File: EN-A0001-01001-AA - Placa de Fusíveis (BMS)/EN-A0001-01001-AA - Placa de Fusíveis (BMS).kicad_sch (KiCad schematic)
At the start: 10 parts

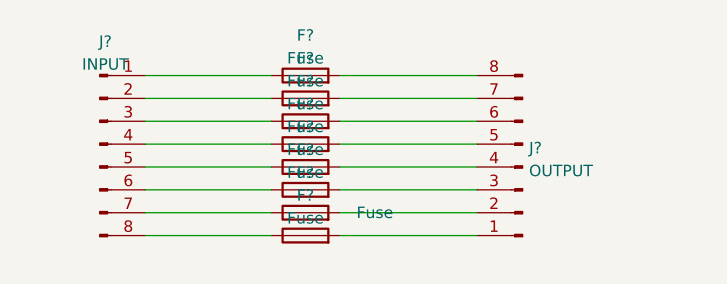
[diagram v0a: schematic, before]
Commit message: ADD: fusiveis
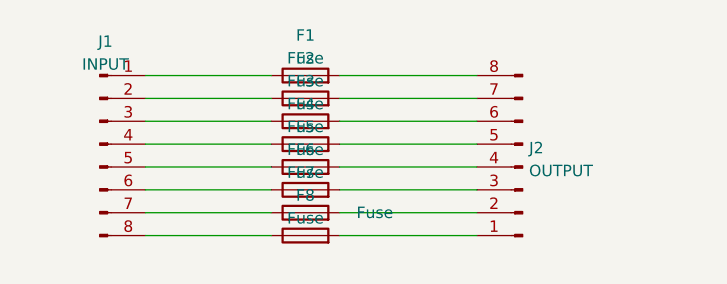
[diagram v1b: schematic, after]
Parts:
- gave numbers to parts that had none: 10
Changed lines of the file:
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@@
   (symbol (lib_id "Device:Fuse") (at 82.55 68.58 90) (unit 1)
     (in_bom yes) (on_board yes) (fields_autoplaced)
-    (property "Reference" "F?" (id 0) (at 82.55 64.1182 90))
+    (property "Reference" "F4" (id 0) (at 82.55 64.1182 90))
     (property "Value" "Fuse" (id 1) (at 82.55 66.6551 90))
     (property "Footprint" "Fuse:Fuseholder_Cylinder-5x20mm_Schurter_0031_8201_Horizontal_Open" (id 2) (at 82.55 70.358 90)
@@
   (symbol (lib_id "Device:Fuse") (at 82.55 76.2 90) (unit 1)
     (in_bom yes) (on_board yes)
-    (property "Reference" "F?" (id 0) (at 82.55 71.7382 90))
+    (property "Reference" "F7" (id 0) (at 82.55 71.7382 90))
     (property "Value" "Fuse" (id 1) (at 90.2626 76.2048 90))
     (property "Footprint" "Fuse:Fuseholder_Cylinder-5x20mm_Schurter_0031_8201_Horizontal_Open" (id 2) (at 82.55 77.978 90)
@@
   (symbol (lib_id "Connector:Conn_01x08_Male") (at 59.69 68.58 0) (unit 1)
     (in_bom yes) (on_board yes) (fields_autoplaced)
-    (property "Reference" "J?" (id 0) (at 60.325 57.184 0))
+    (property "Reference" "J1" (id 0) (at 60.325 57.184 0))
     (property "Value" "INPUT" (id 1) (at 60.325 59.7209 0))
     (property "Footprint" "Connector_PinHeader_2.54mm:PinHeader_1x08_P2.54mm_Vertical" (id 2) (at 59.69 68.58 0)
@@
   (symbol (lib_id "Device:Fuse") (at 82.55 78.74 90) (unit 1)
     (in_bom yes) (on_board yes) (fields_autoplaced)
-    (property "Reference" "F?" (id 0) (at 82.55 74.2782 90))
+    (property "Reference" "F8" (id 0) (at 82.55 74.2782 90))
     (property "Value" "Fuse" (id 1) (at 82.55 76.8151 90))
     (property "Footprint" "Fuse:Fuseholder_Cylinder-5x20mm_Schurter_0031_8201_Horizontal_Open" (id 2) (at 82.55 80.518 90)
@@
   (symbol (lib_id "Connector:Conn_01x08_Male") (at 106.68 71.12 180) (unit 1)
     (in_bom yes) (on_board yes) (fields_autoplaced)
-    (property "Reference" "J?" (id 0) (at 107.3912 69.0153 0)
+    (property "Reference" "J2" (id 0) (at 107.3912 69.0153 0)
       (effects (font (size 1.27 1.27)) (justify right))
     )
@@
   (symbol (lib_id "Device:Fuse") (at 82.55 63.5 90) (unit 1)
     (in_bom yes) (on_board yes) (fields_autoplaced)
-    (property "Reference" "F?" (id 0) (at 82.55 59.0382 90))
+    (property "Reference" "F2" (id 0) (at 82.55 59.0382 90))
     (property "Value" "Fuse" (id 1) (at 82.55 61.5751 90))
     (property "Footprint" "Fuse:Fuseholder_Cylinder-5x20mm_Schurter_0031_8201_Horizontal_Open" (id 2) (at 82.55 65.278 90)
@@
   (symbol (lib_id "Device:Fuse") (at 82.55 66.04 90) (unit 1)
     (in_bom yes) (on_board yes) (fields_autoplaced)
-    (property "Reference" "F?" (id 0) (at 82.55 61.5782 90))
+    (property "Reference" "F3" (id 0) (at 82.55 61.5782 90))
     (property "Value" "Fuse" (id 1) (at 82.55 64.1151 90))
     (property "Footprint" "Fuse:Fuseholder_Cylinder-5x20mm_Schurter_0031_8201_Horizontal_Open" (id 2) (at 82.55 67.818 90)
@@
   (symbol (lib_id "Device:Fuse") (at 82.55 73.66 90) (unit 1)
     (in_bom yes) (on_board yes) (fields_autoplaced)
-    (property "Reference" "F?" (id 0) (at 82.55 69.1982 90))
+    (property "Reference" "F6" (id 0) (at 82.55 69.1982 90))
     (property "Value" "Fuse" (id 1) (at 82.55 71.7351 90))
     (property "Footprint" "Fuse:Fuseholder_Cylinder-5x20mm_Schurter_0031_8201_Horizontal_Open" (id 2) (at 82.55 75.438 90)
@@
   (symbol (lib_id "Device:Fuse") (at 82.55 71.12 90) (unit 1)
     (in_bom yes) (on_board yes) (fields_autoplaced)
-    (property "Reference" "F?" (id 0) (at 82.55 66.6582 90))
+    (property "Reference" "F5" (id 0) (at 82.55 66.6582 90))
     (property "Value" "Fuse" (id 1) (at 82.55 69.1951 90))
     (property "Footprint" "Fuse:Fuseholder_Cylinder-5x20mm_Schurter_0031_8201_Horizontal_Open" (id 2) (at 82.55 72.898 90)
@@
   (symbol (lib_id "Device:Fuse") (at 82.55 60.96 90) (unit 1)
     (in_bom yes) (on_board yes) (fields_autoplaced)
-    (property "Reference" "F?" (id 0) (at 82.55 56.4982 90))
+    (property "Reference" "F1" (id 0) (at 82.55 56.4982 90))
     (property "Value" "Fuse" (id 1) (at 82.55 59.0351 90))
     (property "Footprint" "Fuse:Fuseholder_Cylinder-5x20mm_Schurter_0031_8201_Horizontal_Open" (id 2) (at 82.55 62.738 90)
@@
   )
   (symbol_instances
+    (path "/fbf2aea3-e34c-4957-a6aa-9f886fec1a18"
+      (reference "F1") (unit 1) (value "Fuse") (footprint "Fuse:Fuseholder_Cylinder-5x20mm_Schurter_0031_8201_Horizontal_Open")
+    )
+    (path "/865771ba-3fae-4f9b-afec-ed49718b3127"
+      (reference "F2") (unit 1) (value "Fuse") (footprint "Fuse:Fuseholder_Cylinder-5x20mm_Schurter_0031_8201_Horizontal_Open")
+    )
+    (path "/d5e45496-6b63-4de6-bc9f-385760dffb24"
+      (reference "F3") (unit 1) (value "Fuse") (footprint "Fuse:Fuseholder_Cylinder-5x20mm_Schurter_0031_8201_Horizontal_Open")
+    )
     (path "/0a97a488-0769-4c8f-ae82-484794e08ae9"
-      (reference "F?") (unit 1) (value "Fuse") (footprint "Fuse:Fuseholder_Cylinder-5x20mm_Schurter_0031_8201_Horizontal_Open")
+      (reference "F4") (unit 1) (value "Fuse") (footprint "Fuse:Fuseholder_Cylinder-5x20mm_Schurter_0031_8201_Horizontal_Open")
+    )
+    (path "/f64c8c66-cd89-42a9-a362-abb0b32254f2"
+      (reference "F5") (unit 1) (value "Fuse") (footprint "Fuse:Fuseholder_Cylinder-5x20mm_Schurter_0031_8201_Horizontal_Open")
+    )
+    (path "/ea010cf0-3686-4eef-bddd-6efe2a68261a"
+      (reference "F6") (unit 1) (value "Fuse") (footprint "Fuse:Fuseholder_Cylinder-5x20mm_Schurter_0031_8201_Horizontal_Open")
     )
     (path "/0b4422d2-8244-40fc-bdbc-5eb694d2b36f"
-      (reference "F?") (unit 1) (value "Fuse") (footprint "Fuse:Fuseholder_Cylinder-5x20mm_Schurter_0031_8201_Horizontal_Open")
+      (reference "F7") (unit 1) (value "Fuse") (footprint "Fuse:Fuseholder_Cylinder-5x20mm_Schurter_0031_8201_Horizontal_Open")
     )
     (path "/4dd7e9a4-2de9-44fe-af96-0e860614e093"
-      (reference "F?") (unit 1) (value "Fuse") (footprint "Fuse:Fuseholder_Cylinder-5x20mm_Schurter_0031_8201_Horizontal_Open")
-    )
-    (path "/865771ba-3fae-4f9b-afec-ed49718b3127"
-      (reference "F?") (unit 1) (value "Fuse") (footprint "Fuse:Fuseholder_Cylinder-5x20mm_Schurter_0031_8201_Horizontal_Open")
-    )
-    (path "/d5e45496-6b63-4de6-bc9f-385760dffb24"
-      (reference "F?") (unit 1) (value "Fuse") (footprint "Fuse:Fuseholder_Cylinder-5x20mm_Schurter_0031_8201_Horizontal_Open")
-    )
-    (path "/ea010cf0-3686-4eef-bddd-6efe2a68261a"
-      (reference "F?") (unit 1) (value "Fuse") (footprint "Fuse:Fuseholder_Cylinder-5x20mm_Schurter_0031_8201_Horizontal_Open")
-    )
-    (path "/f64c8c66-cd89-42a9-a362-abb0b32254f2"
-      (reference "F?") (unit 1) (value "Fuse") (footprint "Fuse:Fuseholder_Cylinder-5x20mm_Schurter_0031_8201_Horizontal_Open")
-    )
-    (path "/fbf2aea3-e34c-4957-a6aa-9f886fec1a18"
-      (reference "F?") (unit 1) (value "Fuse") (footprint "Fuse:Fuseholder_Cylinder-5x20mm_Schurter_0031_8201_Horizontal_Open")
+      (reference "F8") (unit 1) (value "Fuse") (footprint "Fuse:Fuseholder_Cylinder-5x20mm_Schurter_0031_8201_Horizontal_Open")
     )
     (path "/182fd5e7-839f-4ea9-a53f-81e4957d72db"
-      (reference "J?") (unit 1) (value "INPUT") (footprint "Connector_PinHeader_2.54mm:PinHeader_1x08_P2.54mm_Vertical")
+      (reference "J1") (unit 1) (value "INPUT") (footprint "Connector_PinHeader_2.54mm:PinHeader_1x08_P2.54mm_Vertical")
     )
     (path "/85e5d25d-024a-449b-9d6c-5672650e1398"
-      (reference "J?") (unit 1) (value "OUTPUT") (footprint "Connector_PinHeader_2.54mm:PinHeader_1x08_P2.54mm_Vertical")
+      (reference "J2") (unit 1) (value "OUTPUT") (footprint "Connector_PinHeader_2.54mm:PinHeader_1x08_P2.54mm_Vertical")
     )
   )

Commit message: ADD: placas
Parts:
- removed J1: INPUT, Connector_PinHeader_2.54mm:PinHeader_1x08_P2.54mm_Vertical, symbol Connector:Conn_01x08_Male
- removed J2: OUTPUT, Connector_PinHeader_2.54mm:PinHeader_1x08_P2.54mm_Vertical, symbol Connector:Conn_01x08_Male
- added F?: Fuse, Fuse:Fuseholder_Cylinder-5x20mm_Schurter_0031_8201_Horizontal_Open, symbol Device:Fuse
- added J? (x2): Conn_01x09_Male, Connector_PinHeader_2.54mm:PinHeader_1x09_P2.54mm_Vertical, symbol Connector:Conn_01x09_Male
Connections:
- net at F4.1: now also J?.4 (Pin_4)
- net at F4.2: now also J?.6 (Pin_6)
- net at F7.1: now also J?.7 (Pin_7)
- net at F7.2: now also J?.3 (Pin_3)
- net at F1.1: now also J?.1 (Pin_1)
- net at F2.1: now also J?.2 (Pin_2)
- net at F3.1: now also J?.3 (Pin_3)
- net at F5.1: now also J?.5 (Pin_5)
- net at F6.1: now also J?.6 (Pin_6)
- net at F8.1: now also J?.8 (Pin_8)
- net at F8.2: now also J?.2 (Pin_2)
- net at F6.2: now also J?.4 (Pin_4)
- net at F5.2: now also J?.5 (Pin_5)
- net at F3.2: now also J?.7 (Pin_7)
- net at F2.2: now also J?.8 (Pin_8)
- net at F1.2: now also J?.9 (Pin_9)
- new net: F?.1, J?.9 (Pin_9)
- new net: F?.2, J?.1 (Pin_1)
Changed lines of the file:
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@@
+    (stroke (width 0) (type default) (color 0 0 0 0))
+  )
+  (wire (pts (xy 64.77 81.28) (xy 78.74 81.28))
     (stroke (width 0) (type default) (color 0 0 0 0))
   )
@@
   )
   (wire (pts (xy 64.77 73.66) (xy 78.74 73.66))
+    (stroke (width 0) (type default) (color 0 0 0 0))
+  )
+  (wire (pts (xy 86.36 81.28) (xy 101.6 81.28))
     (stroke (width 0) (type default) (color 0 0 0 0))
   )
@@
     (pin "2")
   )
-  (symbol (lib_id "Connector:Conn_01x08_Male") (at 59.69 68.58 0) (unit 1)
-    (in_bom yes) (on_board yes) (fields_autoplaced)
-    (property "Reference" "J1" (id 0) (at 60.325 57.184 0))
-    (property "Value" "INPUT" (id 1) (at 60.325 59.7209 0))
-    (property "Footprint" "Connector_PinHeader_2.54mm:PinHeader_1x08_P2.54mm_Vertical" (id 2) (at 59.69 68.58 0)
-      (effects (font (size 1.27 1.27)) hide)
-    )
-    (property "Datasheet" "~" (id 3) (at 59.69 68.58 0)
+  (symbol (lib_id "Device:Fuse") (at 82.55 81.28 90) (unit 1)
+    (in_bom yes) (on_board yes) (fields_autoplaced)
+    (property "Reference" "F?" (id 0) (at 82.55 76.8182 90))
+    (property "Value" "Fuse" (id 1) (at 82.55 79.3551 90))
+    (property "Footprint" "Fuse:Fuseholder_Cylinder-5x20mm_Schurter_0031_8201_Horizontal_Open" (id 2) (at 82.55 83.058 90)
+      (effects (font (size 1.27 1.27)) hide)
+    )
+    (property "Datasheet" "~" (id 3) (at 82.55 81.28 0)
+      (effects (font (size 1.27 1.27)) hide)
+    )
+    (pin "1")
+    (pin "2")
+  )
+  (symbol (lib_id "Connector:Conn_01x09_Male") (at 59.69 71.12 0) (unit 1)
+    (in_bom yes) (on_board yes) (fields_autoplaced)
+    (property "Reference" "J?" (id 0) (at 60.325 55.88 0))
+    (property "Value" "Conn_01x09_Male" (id 1) (at 60.325 58.42 0))
+    (property "Footprint" "Connector_PinHeader_2.54mm:PinHeader_1x09_P2.54mm_Vertical" (id 2) (at 59.69 71.12 0)
+      (effects (font (size 1.27 1.27)) hide)
+    )
+    (property "Datasheet" "~" (id 3) (at 59.69 71.12 0)
       (effects (font (size 1.27 1.27)) hide)
     )
@@
     (pin "7")
     (pin "8")
+    (pin "9")
   )
   (symbol (lib_id "Device:Fuse") (at 82.55 78.74 90) (unit 1)
@@
     (pin "2")
   )
-  (symbol (lib_id "Connector:Conn_01x08_Male") (at 106.68 71.12 180) (unit 1)
-    (in_bom yes) (on_board yes) (fields_autoplaced)
-    (property "Reference" "J2" (id 0) (at 107.3912 69.0153 0)
+  (symbol (lib_id "Connector:Conn_01x09_Male") (at 106.68 71.12 180) (unit 1)
+    (in_bom yes) (on_board yes) (fields_autoplaced)
+    (property "Reference" "J?" (id 0) (at 107.95 69.8499 0)
       (effects (font (size 1.27 1.27)) (justify right))
     )
-    (property "Value" "OUTPUT" (id 1) (at 107.3912 71.5522 0)
+    (property "Value" "Conn_01x09_Male" (id 1) (at 107.95 72.3899 0)
       (effects (font (size 1.27 1.27)) (justify right))
     )
-    (property "Footprint" "Connector_PinHeader_2.54mm:PinHeader_1x08_P2.54mm_Vertical" (id 2) (at 106.68 71.12 0)
+    (property "Footprint" "Connector_PinHeader_2.54mm:PinHeader_1x09_P2.54mm_Vertical" (id 2) (at 106.68 71.12 0)
       (effects (font (size 1.27 1.27)) hide)
     )
@@
     (pin "7")
     (pin "8")
+    (pin "9")
   )
   (symbol (lib_id "Device:Fuse") (at 82.55 63.5 90) (unit 1)
@@
       (reference "F8") (unit 1) (value "Fuse") (footprint "Fuse:Fuseholder_Cylinder-5x20mm_Schurter_0031_8201_Horizontal_Open")
     )
-    (path "/182fd5e7-839f-4ea9-a53f-81e4957d72db"
-      (reference "J1") (unit 1) (value "INPUT") (footprint "Connector_PinHeader_2.54mm:PinHeader_1x08_P2.54mm_Vertical")
-    )
-    (path "/85e5d25d-024a-449b-9d6c-5672650e1398"
-      (reference "J2") (unit 1) (value "OUTPUT") (footprint "Connector_PinHeader_2.54mm:PinHeader_1x08_P2.54mm_Vertical")
-    )
-  )
+    (path "/467ab26a-96c9-46b1-8c9b-3e0d54d21373"
+      (reference "F?") (unit 1) (value "Fuse") (footprint "Fuse:Fuseholder_Cylinder-5x20mm_Schurter_0031_8201_Horizontal_Open")
+    )
+    (path "/46c350bb-7de4-4e81-aafd-4af55e37aab0"
+      (reference "J?") (unit 1) (value "Conn_01x09_Male") (footprint "Connector_PinHeader_2.54mm:PinHeader_1x09_P2.54mm_Vertical")
+    )
+    (path "/63e59f98-801c-4ba0-a31f-3c2327708cfc"
+      (reference "J?") (unit 1) (value "Conn_01x09_Male") (footprint "Connector_PinHeader_2.54mm:PinHeader_1x09_P2.54mm_Vertical")
+    )
+  )
